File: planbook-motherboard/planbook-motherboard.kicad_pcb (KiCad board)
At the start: 6 copper layers, 151 x 88 mm, 443 parts, among them J1 CHARGER, J10 1-2199230-6, J11 Conn_01x33, J12 2199230-5, J13 3-2328724-1, J14 USB_C_Receptacle, J15 CONN_SPK, J16 SAMTEC_TSM-106-02-X-SH-A, J17 POWSW, J18 CONN_HEAD, J2 DM3AT-SF-PEJM5, J20 QWIIC, J3 USB_C_Receptacle, J4 09452812561, J5 SYSCTL, J6 USB_INT1, J7 HDMI_D_1.4, J8 SIM_Card, J9 Conn_01x20, SW1 SW_DIP_x01, SW2 RESET, SW3 RESET, U1 reform2-som-connector, U10 W25Q32JVSS, U11 PCF8523T, U12 AP22615AWU-7, U13 TXS0108EPW, U14 SN74AVC1T45, U15 TPD4E02B04DQA, U16 TPD4E02B04DQA, U17 TPD12S521, U18 TLV320AIC3100, U19 TPD4E02B04DQA, U2 TS3USB30EDGSR, U20 TPD4E02B04DQA, U21 TPD4E02B04DQA, U22 TPD4E02B04DQA, U23 FUSB302BMPX, U24 TXS0108EPW, U25 TUSB8041, U27 TVS2200DRV, U28 LM62460, U29 AP22615AWU-7, U3 LM2830XQMFE/NOPB, U30 TS3USB30EDGSR, U31 TS3USB30EDGSR, U32 AP22615AWU-7, U33 AT24CS02-STUM, U34 PCA9536DP, U35 TMUXHS4446RETR, U36 AP22615AWU-7, U37 TS3USB30EDGSR, U38 CY7C65215-32LTXI, U39 PCA9557PW, U4 TLV75718PDBV, U40 AP22615AWU-7, U41 AP22615AWU-7, U42 TPS560430X3FDBVR, U5 LM73100RPWR, U6 LM62460, U7 74LVC1G34, U8 RP2040, U9 TPS7A0533PDBZ, Y1 24MHz, Y2 12MHz 12pF, Y3 32.768 kHz

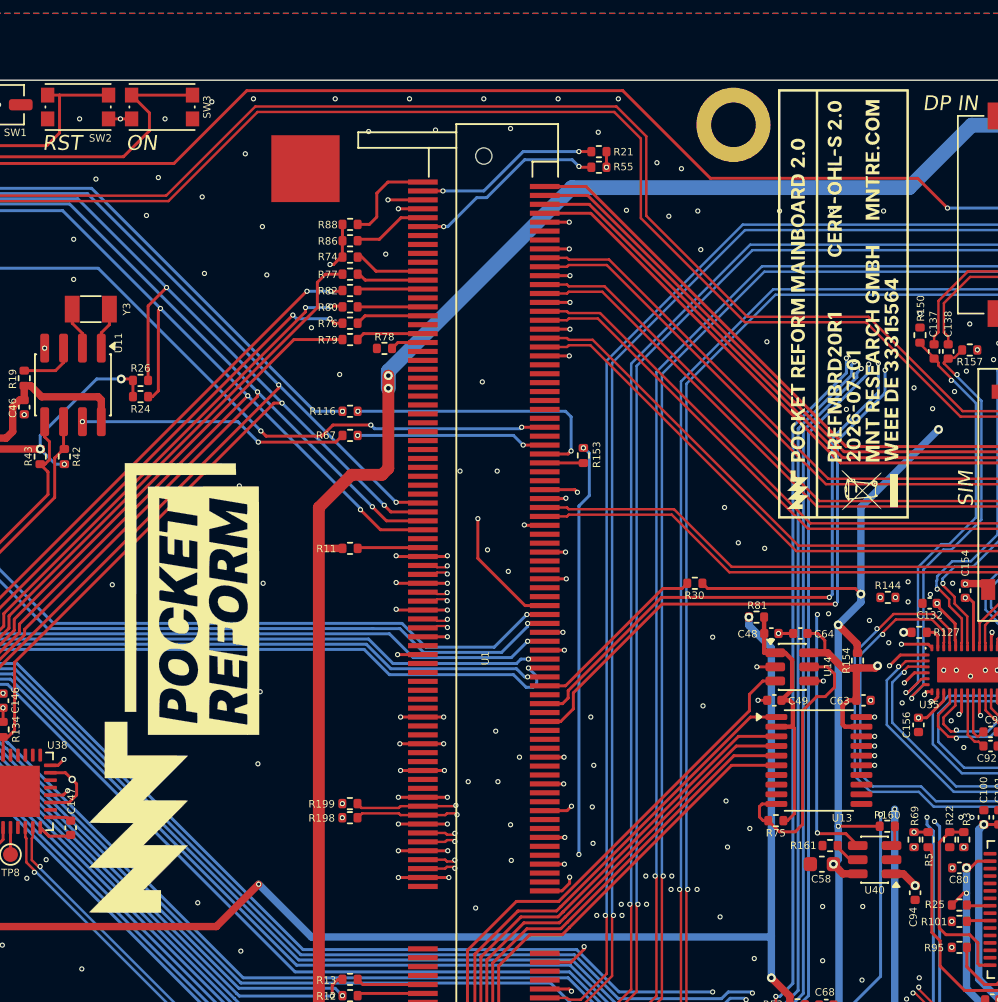
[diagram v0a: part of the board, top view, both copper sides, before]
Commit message: Replace PCB logos with PlanBook text
- Removed all badge footprint graphics from PCB files
- Added "PlanBook" text in same positions with default font
- Updated footprint library files to use simple text instead of complex logos
- Updated schematic footprint references to empty strings
- Text uses font size 1.5x1.5 with thickness 0.3
- Maintained exact positions and rotations from original footprints

Generated with [Devin](https://devin.ai)

Co-Authored-By: Devin <158243242+devin-ai-integration[bot]@users.noreply.github.com>
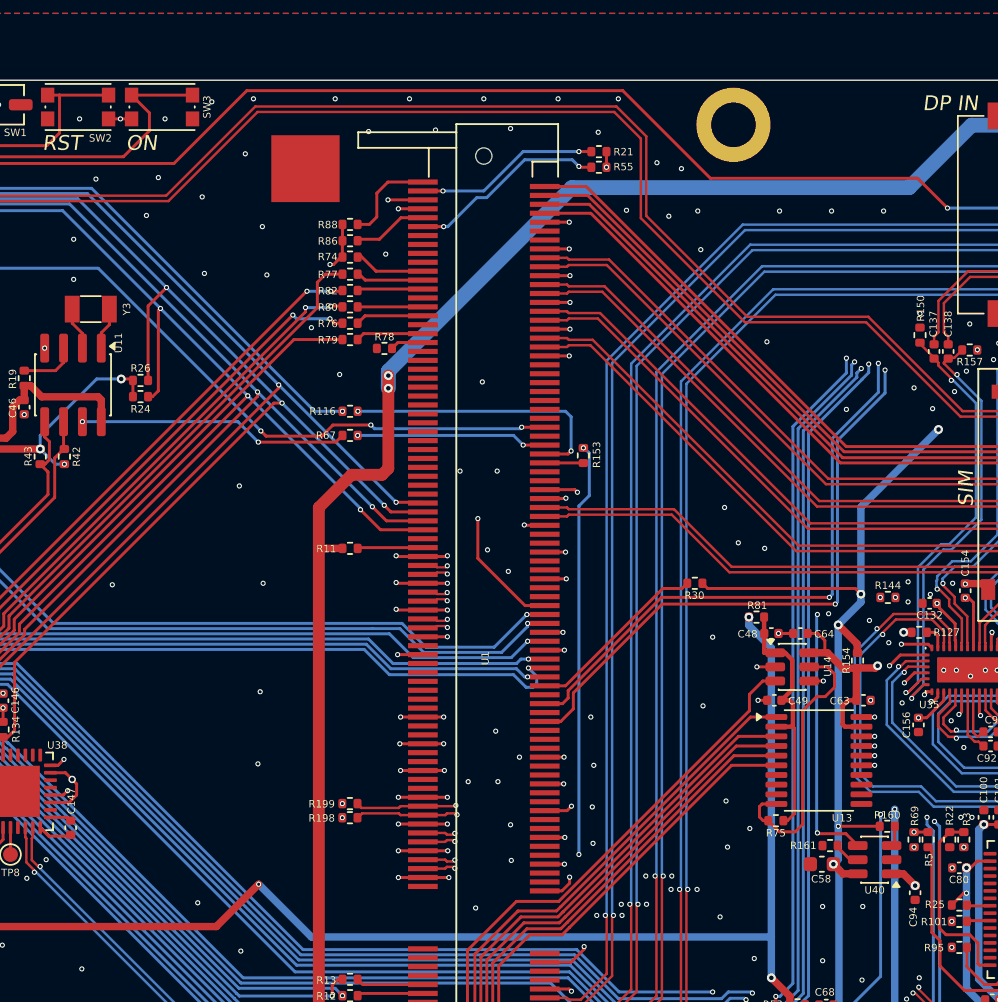
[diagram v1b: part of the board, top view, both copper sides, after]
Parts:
- removed GFX1: MountingHole, footprints:planbook
- removed GFX2: MountingHole, footprints:pref-motherboard-badge
